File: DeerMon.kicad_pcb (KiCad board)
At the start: 4 copper layers, 30 x 45 mm, 53 parts, among them J1 TYPE-C-31-M-12, J2 ZJY144S025, J3 GPIO, Q1 PUMH4, Q2 2N7002, SW1 BOOT, SW2 EN, U1 CP2102N-A02-GQFN24R, U2 BCT3220ELA-TR, U3 SPX3819M5-L-3-3, U4 ESP32-PICO-V3-02

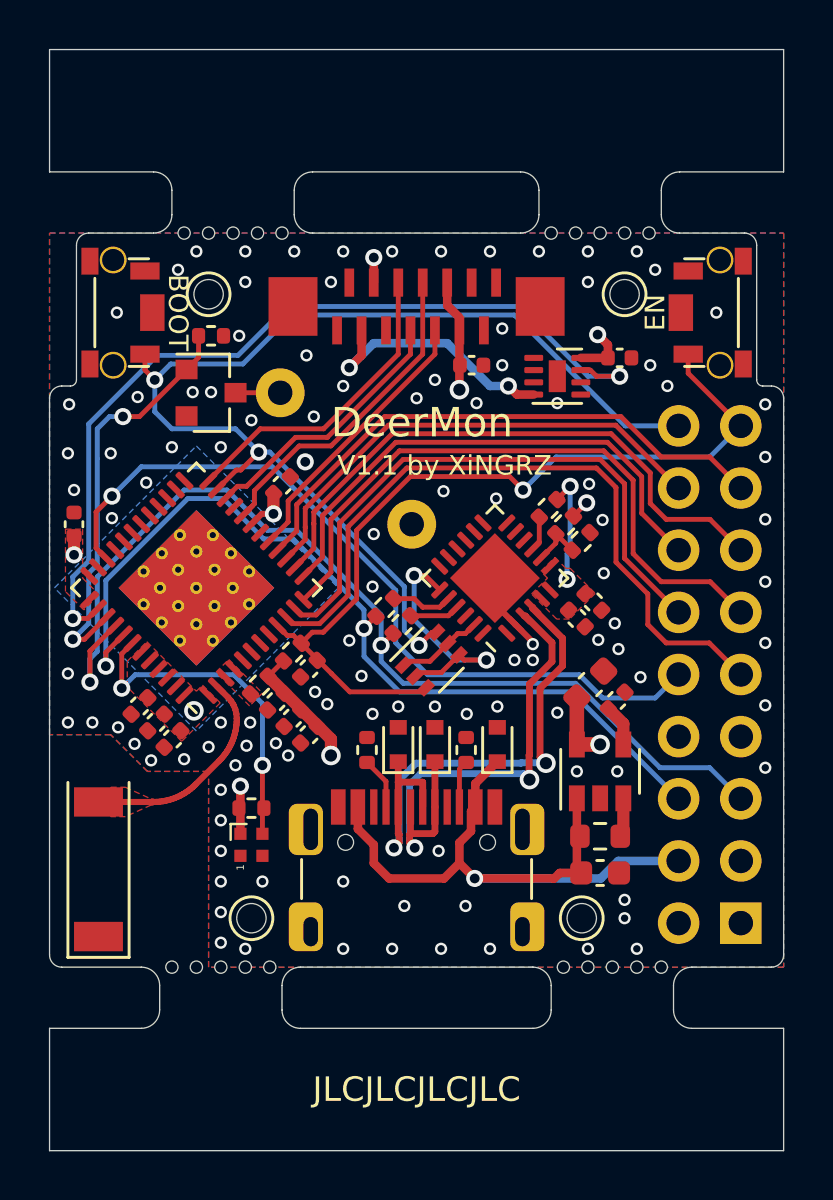
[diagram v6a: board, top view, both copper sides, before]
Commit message: Use CH343P instead of CP2102N-A02-GQFN24R
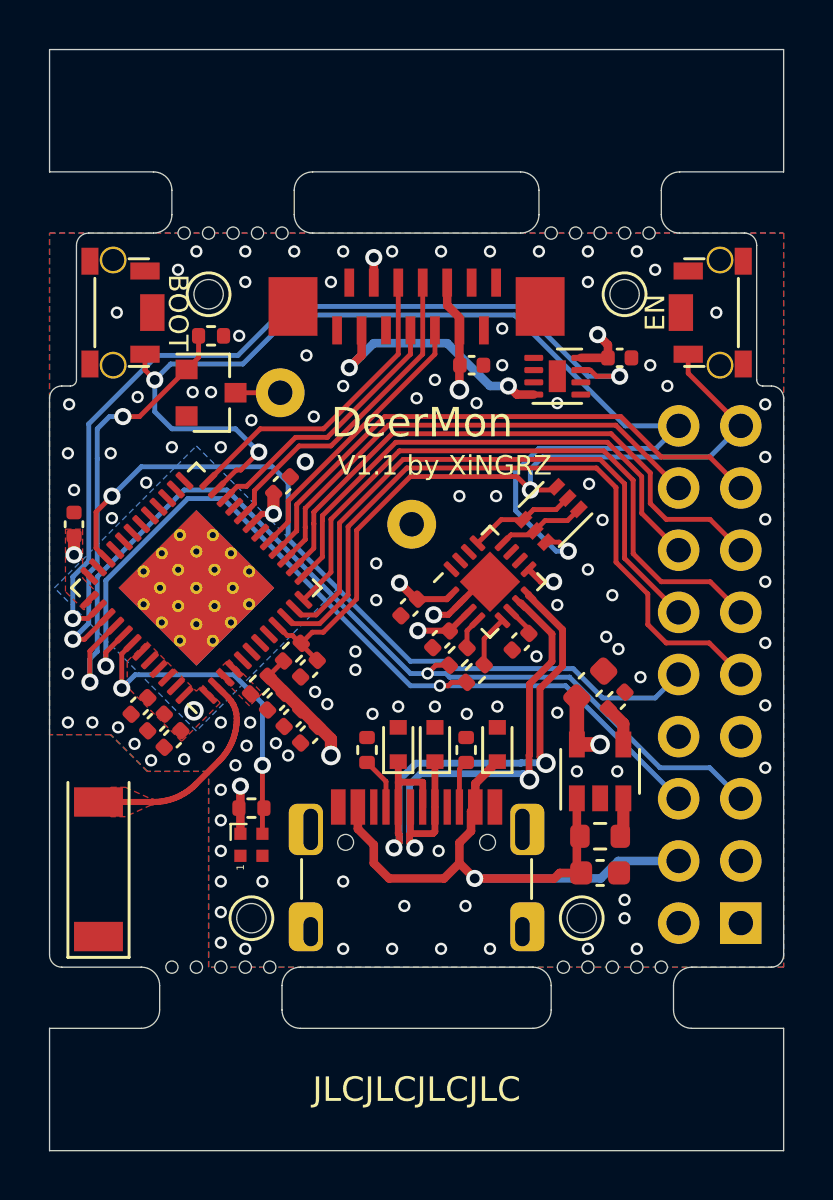
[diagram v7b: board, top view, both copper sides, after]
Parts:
- removed R1: 22.1K(1%), Resistor_SMD:R_0402_1005Metric
- removed R2: 47.5K(1%), Resistor_SMD:R_0402_1005Metric
- removed R5: 1K, Resistor_SMD:R_0402_1005Metric
- added C17: 0.1uF, Capacitor_SMD:C_0402_1005Metric, F.Cu at (69.2, 66.7)
- C1: value 4.7uF -> 0.1uF
- U1: value CP2102N-A02-GQFN24R -> CH343P; footprint Package_DFN_QFN:QFN-24-1EP_4x4mm_P0.5mm_EP2.6x2.6mm -> Package_DFN_QFN:WQFN-16-1EP_3x3mm_P0.5mm_EP1.75x1.75mm
- moved Q1 7.71 mm to (70.5, 61.5), turned to 225 degrees
- moved C1 7.53 mm to (64.7, 65.3), turned to 225 degrees
- moved C2 5.61 mm to (66.0, 66.6), turned to 225 degrees
- moved R7 4.58 mm to (67.4, 68.0)
- moved R8 2.64 mm to (66.7, 67.3)
- moved U1 0.25 mm to (68.0, 64.2), turned to 45 degrees
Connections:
- C2 pad 1: +3V3 -> +5V
- U1 pad 1: (no net) -> +3V3
- U1 pad 12: (no net) -> /DTR
- U1 pad 13: (no net) -> /RTS
- U1 pad 17: (no net) -> GND
- U1 pad 3: /D+ -> +5V
- U1 pad 4: /D- -> /USB_TX
- U1 pad 5: +3V3 -> /USB_RX
- U1 pad 6: +3V3 -> Net-(C17-Pad1)
- U1 pad 7: +3V3 -> /D+
- U1 pad 8: Net-(R1-Pad1) -> /D-
- U1 pad 9: Net-(R5-Pad1) -> +5V
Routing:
- net +5V: track 53.1 -> 66.6 mm, vias 2 -> 3
- net /RTS: track 10.1 -> 4.45 mm, vias 2 -> 0
- net +3V3: track 114.3 -> 110.8 mm, vias 11 -> 10
- net /EN: track 34.8 -> 31.4 mm
- net Net-(R1-Pad1): track 2.17 -> 0.00 mm
- net Net-(R5-Pad1): track 1.41 -> 0.00 mm
- net Net-(C17-Pad1): track 0.00 -> 1.19 mm
- net /BOOT: track 46.0 -> 47.1 mm
- net /ESP_RX: track 42.0 -> 41.2 mm
- net /USB_TX: track 2.04 -> 1.29 mm
- net /ESP_TX: track 36.8 -> 36.1 mm
- net /D-: track 22.2 -> 22.8 mm
- net /D+: track 21.1 -> 21.7 mm

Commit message: Better layout
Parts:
- moved C1 0.50 mm to (64.2, 65.3)
- moved C17 0.50 mm to (68.8, 66.7)
- moved C2 0.50 mm to (65.5, 66.6)
- moved Q1 0.50 mm to (70.0, 61.5)
- moved R7 0.50 mm to (66.9, 68.0)
- moved R8 0.50 mm to (66.2, 67.3)
- moved U1 0.50 mm to (67.5, 64.2)
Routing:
- net /BOOT: track 47.1 -> 44.3 mm
- net /IO5: track 32.8 -> 31.5 mm
- net /EN: track 31.4 -> 30.1 mm
- net +5V: track 66.6 -> 67.4 mm
- net GND: vias 109 -> 112
